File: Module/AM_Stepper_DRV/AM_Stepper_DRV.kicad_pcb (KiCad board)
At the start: 2 copper layers, 20.3 x 30.5 mm, 15 parts, among them J1 CONN_01X04, J2 CONN_01X02, M1 Aktuator_Module, U1 DRV8811

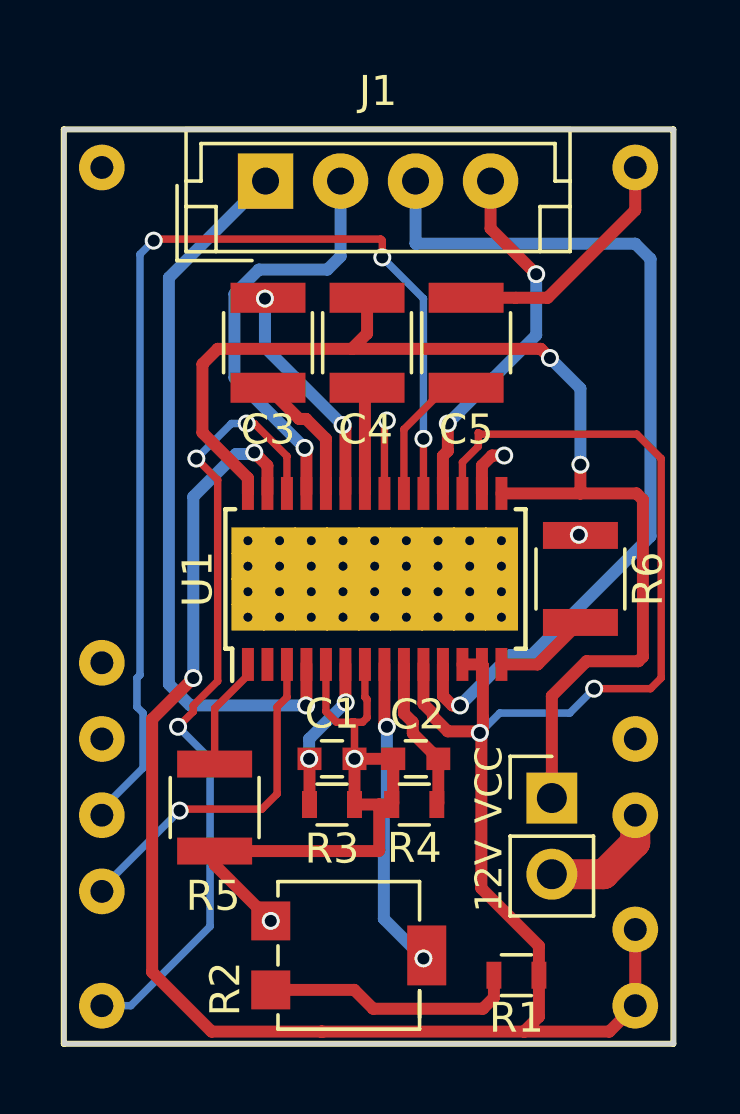
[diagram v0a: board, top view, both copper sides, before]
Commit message: Added actuator board drill and gerber
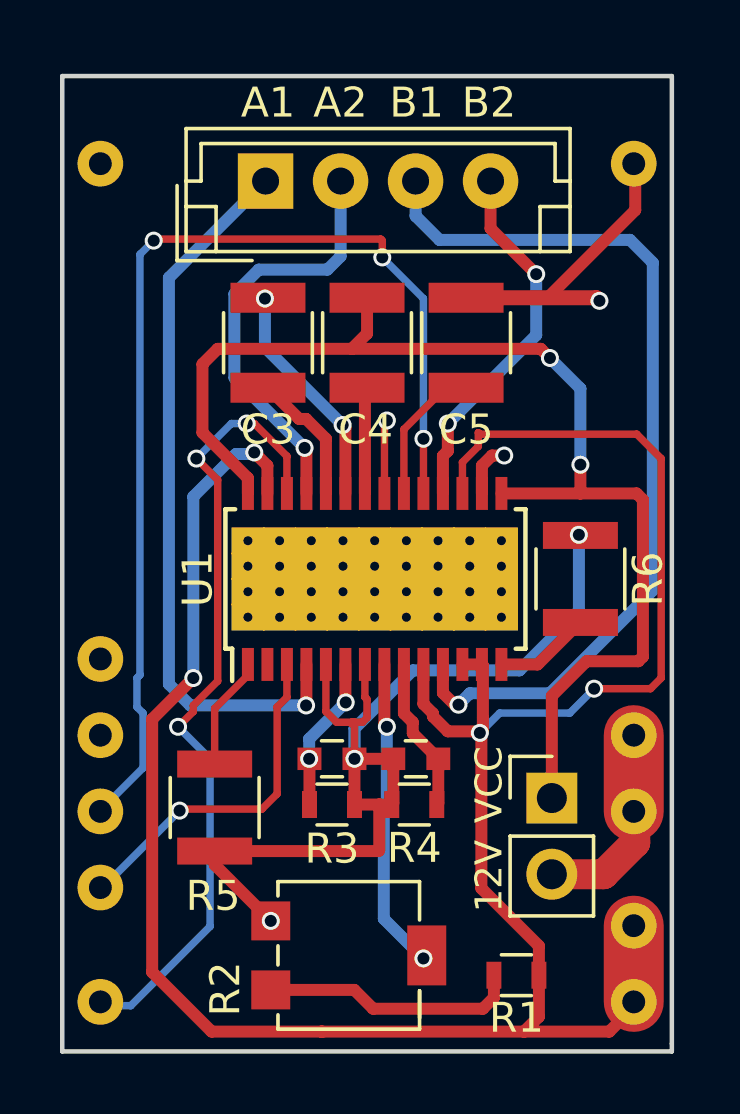
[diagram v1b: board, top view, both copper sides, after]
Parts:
- added G***: LOGO, Hardware:EP_Logo_3, B.Cu at (194.6, 102.6)
- moved M1 0.14 mm to (185.9, 109.6)
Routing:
- net GND: track 34.8 -> 51.9 mm, vias 5 -> 6
- net 5V: track 81.1 -> 83.6 mm
- net Net-(J2-Pad2): track 4.13 -> 6.67 mm
- net Net-(J1-Pad3): track 29.8 -> 30.3 mm
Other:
- board size 20.3 x 30.5 mm -> 20.3 x 32.5 mm
- board text added: "A1"
- board text added: "A2"
- board text added: "B1"
- board text added: "B2"
